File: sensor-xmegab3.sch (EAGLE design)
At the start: 46 parts, among them K1 SP6029TOP, M1 NRF24L01P-M, M2 DHT22-NP, Q1 IRLML2502, Q2 IRLML2502, U1 MCP1640C, X1 serial, X2 SPI/1W, X3 I2C, X4 ADC, X6 PDI

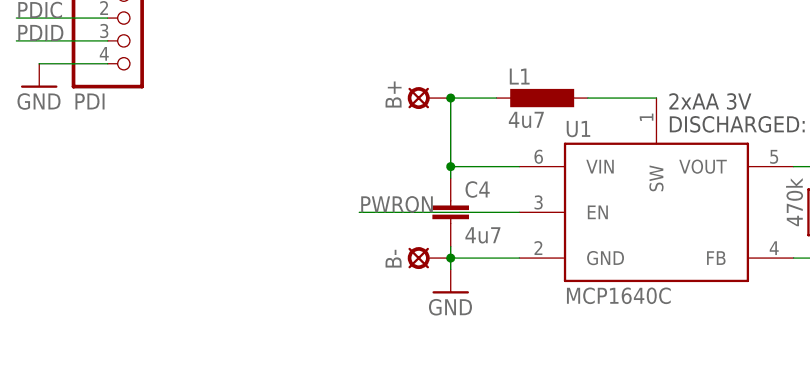
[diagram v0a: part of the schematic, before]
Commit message: pulldown for boostup enable line
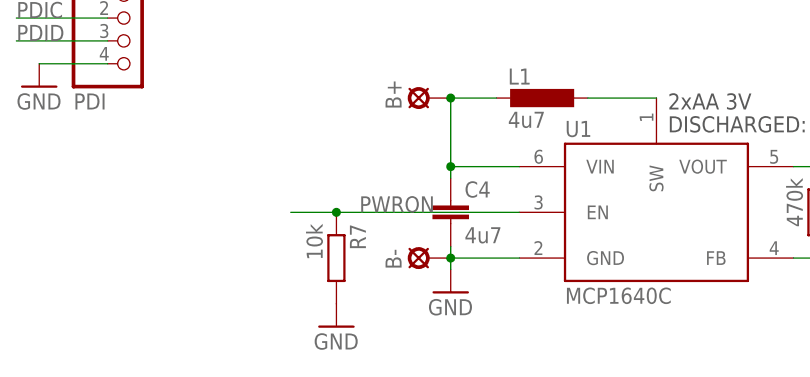
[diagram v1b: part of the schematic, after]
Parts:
- added R7: 10k, rcl:R-EU_R0603
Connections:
- net GND: now also R7.2
- net PWRON: now also R7.1
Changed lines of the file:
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@@
 <setting verticaltext="up"/>
 </settings>
-<grid distance="1.27" unitdist="mm" unit="mm" style="lines" multiple="1" display="yes" altdistance="635" altunitdist="mic" altunit="mic"/>
+<grid distance="0.1" unitdist="inch" unit="mm" style="lines" multiple="1" display="yes" altdistance="0.01" altunitdist="inch" altunit="mm"/>
 <layers>
 <layer number="1" name="Top" color="4" fill="1" visible="no" active="no"/>
@@
 <part name="X6" library="pinhead-mod" deviceset="PINHD-1X4" device="_2.54" value="PDI"/>
 <part name="Q1" library="mosfet" deviceset="IRLML2502" device=""/>
+<part name="R7" library="rcl" deviceset="R-EU_" device="R0603" value="10k"/>
+<part name="GND7" library="supply1" deviceset="GND" device=""/>
 </parts>
 <sheets>
@@
 <instance part="X6" gate="A" x="63.5" y="36.83"/>
 <instance part="Q1" gate="G$1" x="208.28" y="116.84"/>
+<instance part="R7" gate="G$1" x="86.36" y="12.7" rot="R270"/>
+<instance part="GND7" gate="1" x="86.36" y="5.08"/>
 </instances>
 <busses>
@@
 <pinref part="GND6" gate="1" pin="GND"/>
 </segment>
+<segment>
+<pinref part="R7" gate="G$1" pin="2"/>
+<pinref part="GND7" gate="1" pin="GND"/>
+</segment>
 </net>
 <net name="VCC" class="0">
@@
 <segment>
 <pinref part="U1" gate="G$1" pin="EN"/>
-<wire x1="106.68" y1="17.78" x2="88.9" y2="17.78" width="0.1524" layer="91"/>
+<wire x1="106.68" y1="17.78" x2="86.36" y2="17.78" width="0.1524" layer="91"/>
 <label x="88.9" y="17.78" size="1.778" layer="95"/>
-</segment>
-</net>
+<pinref part="R7" gate="G$1" pin="1"/>
+<wire x1="86.36" y1="17.78" x2="81.28" y2="17.78" width="0.1524" layer="91"/>
+<junction x="86.36" y="17.78"/>
+</segment>
+</net>

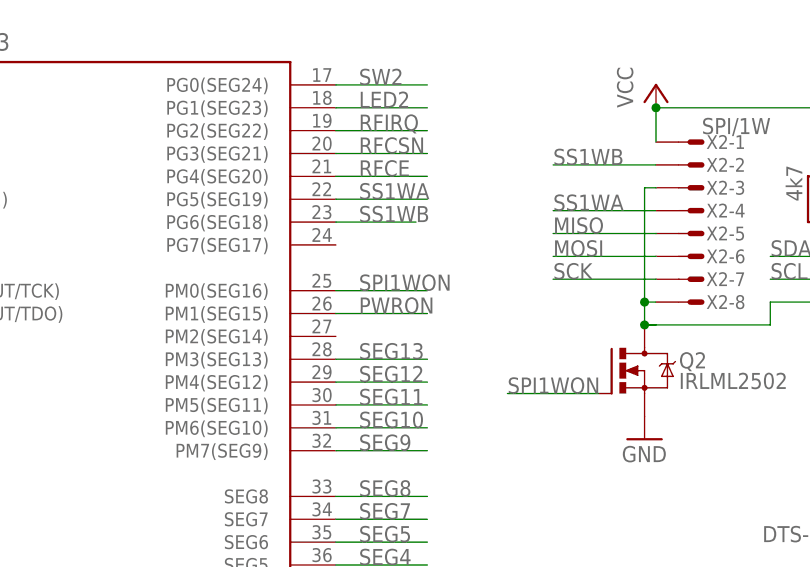
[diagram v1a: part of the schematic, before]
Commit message: free seg14/15, can't be used with lcd in use
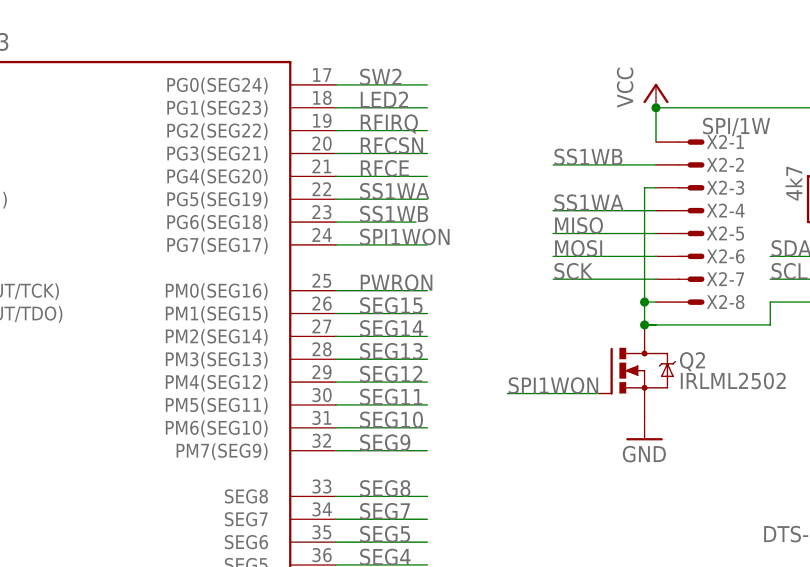
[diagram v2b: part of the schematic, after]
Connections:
- new net SEG14: UC1.PM2(SEG14)
- new net SEG15: UC1.PM1(SEG15)
- net PWRON: now also UC1.PM0(SEG16); no longer UC1.PM1(SEG15)
- net SPI1WON: now also UC1.PG7(SEG17); no longer UC1.PM0(SEG16)
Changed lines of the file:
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@@
 <setting verticaltext="up"/>
 </settings>
-<grid distance="0.1" unitdist="inch" unit="mm" style="lines" multiple="1" display="yes" altdistance="0.01" altunitdist="inch" altunit="mm"/>
+<grid distance="1.27" unitdist="mm" unit="mm" style="lines" multiple="1" display="yes" altdistance="635" altunitdist="mic" altunit="mic"/>
 <layers>
 <layer number="1" name="Top" color="4" fill="1" visible="no" active="no"/>
@@
 <net name="PWRON" class="0">
 <segment>
-<label x="104.14" y="130.81" size="1.778" layer="95"/>
-<pinref part="UC1" gate="G$1" pin="PM1(SEG15)"/>
-<wire x1="101.6" y1="130.81" x2="111.76" y2="130.81" width="0.1524" layer="91"/>
+<label x="104.14" y="133.35" size="1.778" layer="95"/>
+<wire x1="101.6" y1="133.35" x2="111.76" y2="133.35" width="0.1524" layer="91"/>
+<pinref part="UC1" gate="G$1" pin="PM0(SEG16)"/>
 </segment>
 <segment>
@@
 </segment>
 <segment>
-<label x="104.14" y="133.35" size="1.778" layer="95"/>
-<wire x1="101.6" y1="133.35" x2="111.76" y2="133.35" width="0.1524" layer="91"/>
-<pinref part="UC1" gate="G$1" pin="PM0(SEG16)"/>
+<label x="104.14" y="138.43" size="1.778" layer="95"/>
+<wire x1="101.6" y1="138.43" x2="111.76" y2="138.43" width="0.1524" layer="91"/>
+<pinref part="UC1" gate="G$1" pin="PG7(SEG17)"/>
 </segment>
 </net>
@@
 </segment>
 </net>
+<net name="SEG14" class="0">
+<segment>
+<pinref part="UC1" gate="G$1" pin="PM2(SEG14)"/>
+<wire x1="101.6" y1="128.27" x2="111.76" y2="128.27" width="0.1524" layer="91"/>
+<label x="104.14" y="128.27" size="1.778" layer="95"/>
+</segment>
+</net>
+<net name="SEG15" class="0">
+<segment>
+<pinref part="UC1" gate="G$1" pin="PM1(SEG15)"/>
+<wire x1="111.76" y1="130.81" x2="101.6" y2="130.81" width="0.1524" layer="91"/>
+<label x="104.14" y="130.81" size="1.778" layer="95"/>
+</segment>
+</net>

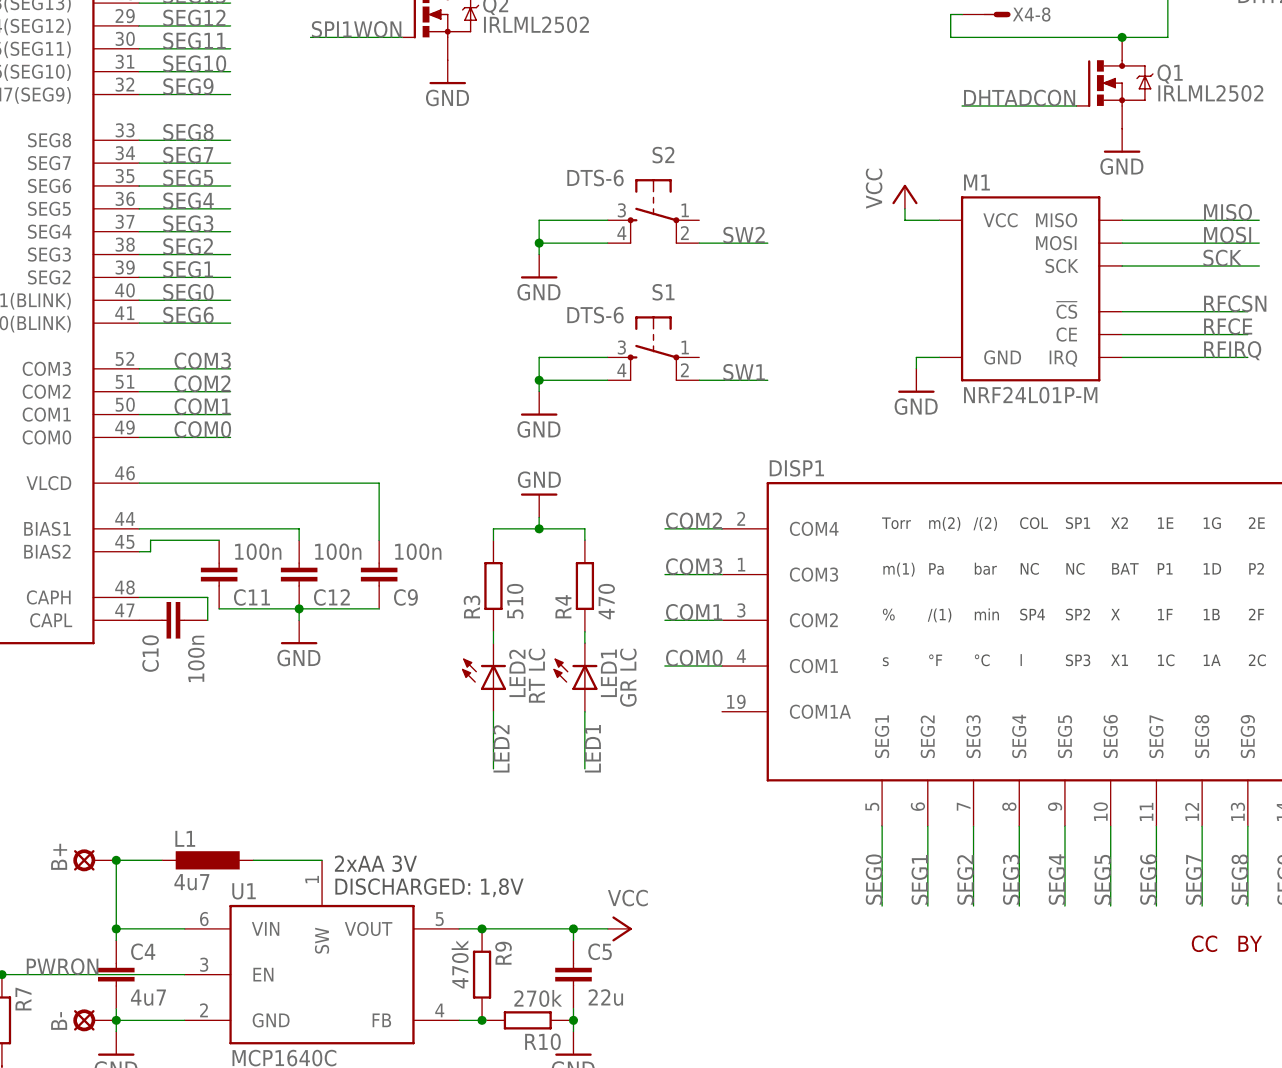
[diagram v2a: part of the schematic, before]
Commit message: reassign display pins
    fixes #1
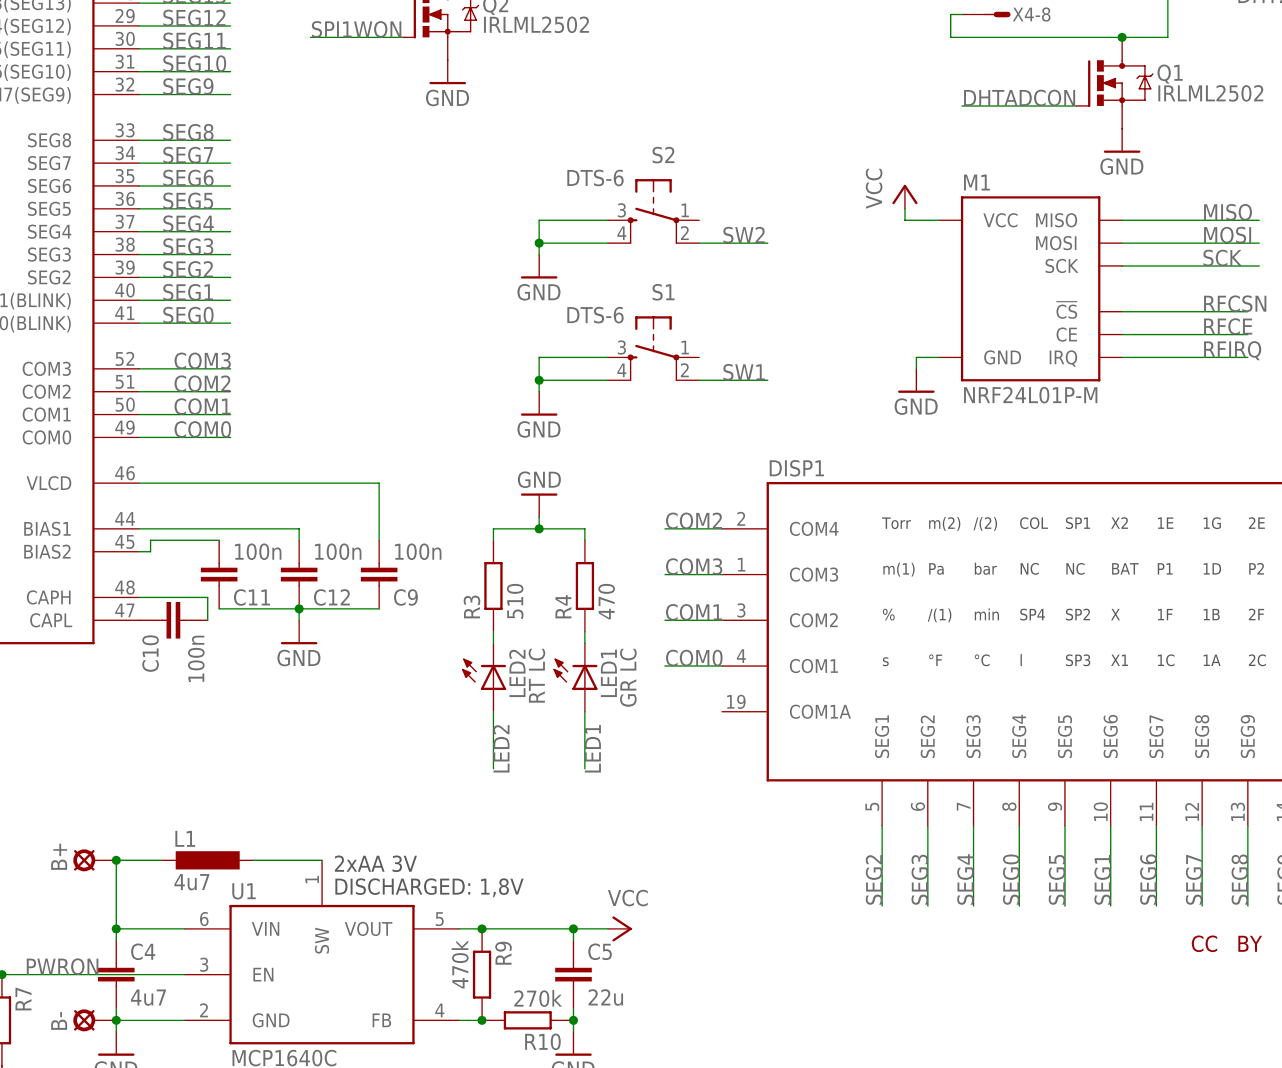
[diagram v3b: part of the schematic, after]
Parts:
- X5: value (none) -> USB
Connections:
- net SEG0: now also DISP1.SEG4, UC1.SEG0(BLINK); no longer DISP1.SEG1, UC1.SEG1(BLINK)
- net SEG1: now also DISP1.SEG6, UC1.SEG1(BLINK); no longer DISP1.SEG2, UC1.SEG2
- net SEG2: now also DISP1.SEG1, UC1.SEG2; no longer DISP1.SEG3, UC1.SEG3
- net SEG3: now also DISP1.SEG2, UC1.SEG3; no longer DISP1.SEG4, UC1.SEG4
- net SEG4: now also DISP1.SEG3, UC1.SEG4; no longer DISP1.SEG5, UC1.SEG5
- net SEG5: now also DISP1.SEG5, UC1.SEG5; no longer DISP1.SEG6, UC1.SEG6
- net SEG6: now also UC1.SEG6; no longer UC1.SEG0(BLINK)
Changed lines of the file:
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@@
 <part name="P+3" library="supply1" deviceset="VCC" device=""/>
 <part name="GND1" library="supply1" deviceset="GND" device=""/>
-<part name="X5" library="con-usb" deviceset="USB" device="-MB-S"/>
+<part name="X5" library="con-usb" deviceset="USB" device="-MB-S" value="USB"/>
 <part name="GND13" library="supply1" deviceset="GND" device=""/>
 <part name="R5" library="rcl" deviceset="R-EU_" device="R0603" value="15k"/>
@@
 <net name="SEG0" class="0">
 <segment>
-<pinref part="DISP1" gate="G$1" pin="SEG1"/>
-<wire x1="184.15" y1="25.4" x2="184.15" y2="34.29" width="0.1524" layer="91"/>
-<label x="184.15" y="25.4" size="1.778" layer="95" rot="R90"/>
+<wire x1="199.39" y1="25.4" x2="199.39" y2="34.29" width="0.1524" layer="91"/>
+<label x="199.39" y="25.4" size="1.778" layer="95" rot="R90"/>
+<pinref part="DISP1" gate="G$1" pin="SEG4"/>
+</segment>
+<segment>
+<wire x1="101.6" y1="90.17" x2="111.76" y2="90.17" width="0.1524" layer="91"/>
+<label x="104.14" y="90.17" size="1.778" layer="95"/>
+<pinref part="UC1" gate="G$1" pin="SEG0(BLINK)"/>
+</segment>
+</net>
+<net name="SEG1" class="0">
+<segment>
+<wire x1="209.55" y1="25.4" x2="209.55" y2="34.29" width="0.1524" layer="91"/>
+<label x="209.55" y="25.4" size="1.778" layer="95" rot="R90"/>
+<pinref part="DISP1" gate="G$1" pin="SEG6"/>
 </segment>
 <segment>
@@
 </segment>
 </net>
-<net name="SEG1" class="0">
-<segment>
-<pinref part="DISP1" gate="G$1" pin="SEG2"/>
-<wire x1="189.23" y1="25.4" x2="189.23" y2="34.29" width="0.1524" layer="91"/>
-<label x="189.23" y="25.4" size="1.778" layer="95" rot="R90"/>
+<net name="SEG2" class="0">
+<segment>
+<wire x1="184.15" y1="25.4" x2="184.15" y2="34.29" width="0.1524" layer="91"/>
+<label x="184.15" y="25.4" size="1.778" layer="95" rot="R90"/>
+<pinref part="DISP1" gate="G$1" pin="SEG1"/>
 </segment>
 <segment>
@@
 </segment>
 </net>
-<net name="SEG2" class="0">
-<segment>
-<pinref part="DISP1" gate="G$1" pin="SEG3"/>
-<wire x1="194.31" y1="34.29" x2="194.31" y2="25.4" width="0.1524" layer="91"/>
-<label x="194.31" y="25.4" size="1.778" layer="95" rot="R90"/>
+<net name="SEG3" class="0">
+<segment>
+<wire x1="189.23" y1="25.4" x2="189.23" y2="34.29" width="0.1524" layer="91"/>
+<label x="189.23" y="25.4" size="1.778" layer="95" rot="R90"/>
+<pinref part="DISP1" gate="G$1" pin="SEG2"/>
 </segment>
 <segment>
@@
 </segment>
 </net>
-<net name="SEG3" class="0">
-<segment>
-<pinref part="DISP1" gate="G$1" pin="SEG4"/>
-<wire x1="199.39" y1="25.4" x2="199.39" y2="34.29" width="0.1524" layer="91"/>
-<label x="199.39" y="25.4" size="1.778" layer="95" rot="R90"/>
+<net name="SEG4" class="0">
+<segment>
+<label x="194.31" y="25.4" size="1.778" layer="95" rot="R90"/>
+<wire x1="194.31" y1="34.29" x2="194.31" y2="25.4" width="0.1524" layer="91"/>
+<pinref part="DISP1" gate="G$1" pin="SEG3"/>
 </segment>
 <segment>
@@
 </segment>
 </net>
-<net name="SEG4" class="0">
-<segment>
-<pinref part="DISP1" gate="G$1" pin="SEG5"/>
+<net name="SEG5" class="0">
+<segment>
 <wire x1="204.47" y1="25.4" x2="204.47" y2="34.29" width="0.1524" layer="91"/>
 <label x="204.47" y="25.4" size="1.778" layer="95" rot="R90"/>
+<pinref part="DISP1" gate="G$1" pin="SEG5"/>
 </segment>
 <segment>
@@
 </segment>
 </net>
-<net name="SEG5" class="0">
-<segment>
-<pinref part="DISP1" gate="G$1" pin="SEG6"/>
-<wire x1="209.55" y1="25.4" x2="209.55" y2="34.29" width="0.1524" layer="91"/>
-<label x="209.55" y="25.4" size="1.778" layer="95" rot="R90"/>
+<net name="SEG6" class="0">
+<segment>
+<wire x1="214.63" y1="25.4" x2="214.63" y2="34.29" width="0.1524" layer="91"/>
+<label x="214.63" y="25.4" size="1.778" layer="95" rot="R90"/>
+<pinref part="DISP1" gate="G$1" pin="SEG7"/>
 </segment>
 <segment>
@@
 </segment>
 </net>
-<net name="SEG6" class="0">
-<segment>
-<pinref part="DISP1" gate="G$1" pin="SEG7"/>
-<wire x1="214.63" y1="25.4" x2="214.63" y2="34.29" width="0.1524" layer="91"/>
-<label x="214.63" y="25.4" size="1.778" layer="95" rot="R90"/>
-</segment>
-<segment>
-<wire x1="101.6" y1="90.17" x2="111.76" y2="90.17" width="0.1524" layer="91"/>
-<label x="104.14" y="90.17" size="1.778" layer="95"/>
-<pinref part="UC1" gate="G$1" pin="SEG0(BLINK)"/>
-</segment>
-</net>
 <net name="SEG7" class="0">
 <segment>
-<pinref part="DISP1" gate="G$1" pin="SEG8"/>
 <wire x1="219.71" y1="25.4" x2="219.71" y2="34.29" width="0.1524" layer="91"/>
 <label x="219.71" y="25.4" size="1.778" layer="95" rot="R90"/>
+<pinref part="DISP1" gate="G$1" pin="SEG8"/>
 </segment>
 <segment>
@@
 <net name="SEG8" class="0">
 <segment>
-<pinref part="DISP1" gate="G$1" pin="SEG9"/>
 <wire x1="224.79" y1="25.4" x2="224.79" y2="34.29" width="0.1524" layer="91"/>
 <label x="224.79" y="25.4" size="1.778" layer="95" rot="R90"/>
-</segment>
-<segment>
+<pinref part="DISP1" gate="G$1" pin="SEG9"/>
+</segment>
+<segment>
